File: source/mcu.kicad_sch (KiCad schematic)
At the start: 13 parts

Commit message: Add files via upload
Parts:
- gave numbers to parts that had none: 13
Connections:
- net at C72.1, U11.6 (PH1-OSC_OUT): now also Y1.3
- net PB2: now reaches U11.28 (PB2-BOOT1)
- net PA15: now reaches U11.50 (PA15(JTDI))
- net ADC_15: no longer names the net of U11.25 (PC5(ADC12_IN15))
- net ADC_TEMP2: no longer names the net of U11.26 (PB0(ADC12_IN8))
- net ADC_TEMP3: no longer names the net of U11.27 (PB1(ADC12_IN9))
- net MISO_ADC_EXT2: no longer names the net of U11.22 (PA6(ADC12_IN6))
- net PC10_UART_TX: no longer names the net of U11.51 (PC10)
- net PC11_UART_RX: no longer names the net of U11.52 (PC11)
- net PC12: no longer names the net of U11.53 (PC12)
- net PC9: no longer names the net of U11.40 (PC9)
- net RX_SDA_NSS: no longer names the net of U11.20 (PA4(ADC12_IN4/DAC1_OUT))
- net RX_SDA_NSS: no longer U11.30 (PB11)
- net SCK_ADC_EXT: no longer names the net of U11.21 (PA5(ADC12_IN5/DAC2_OUT))
- net TX_SCL_MOSI: no longer names the net of U11.23 (PA7(ADC12_IN7))
- net TX_SCL_MOSI: no longer U11.29 (PB10)
- no-connect marks 9 -> 20

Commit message: Changes suggested by mxlemming, Elwin and hackey on Discord
New power supplies and using other op-amps for current sense
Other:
- note added: "F-Of-C"
- note removed: "Free-Of-Charge"
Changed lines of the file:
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@@
     (effects (font (size 1.27 1.27)) (justify left bottom))
   )
-  (text "Free-Of-Charge" (at 187.96 191.77 0)
+  (text "F-Of-C" (at 187.96 191.77 0)
     (effects (font (size 2.54 2.54)) (justify left bottom))
   )

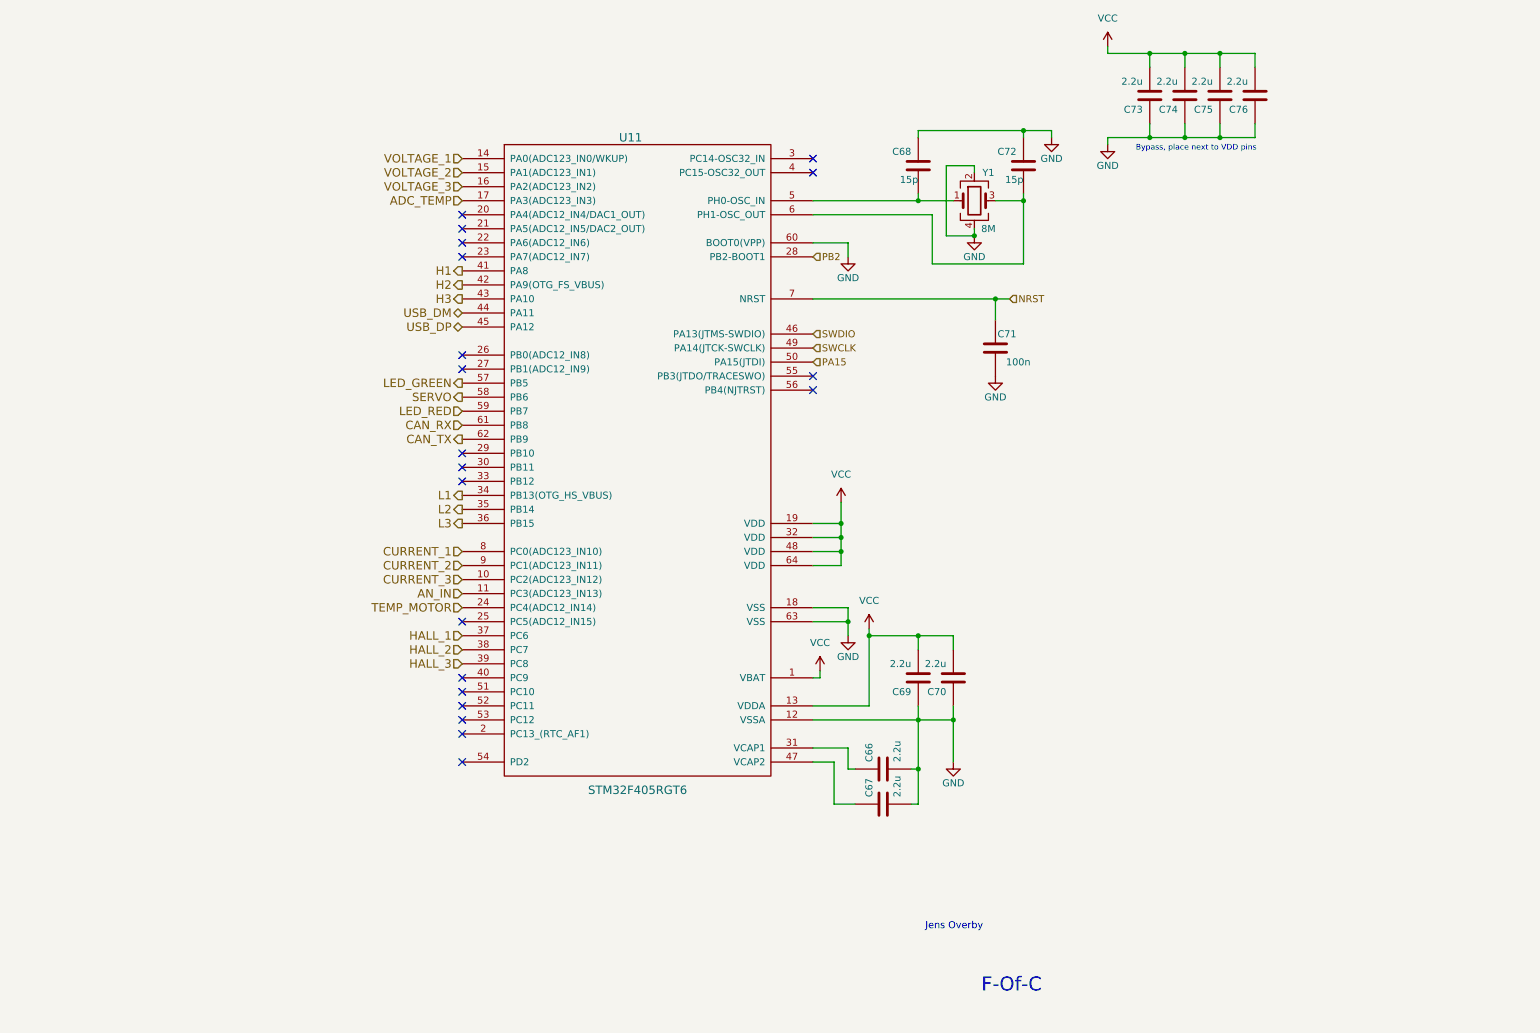
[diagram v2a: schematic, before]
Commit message: First attempt of layout
It's a rats nest. Will have to remove some connections temporarily for the first prototype.
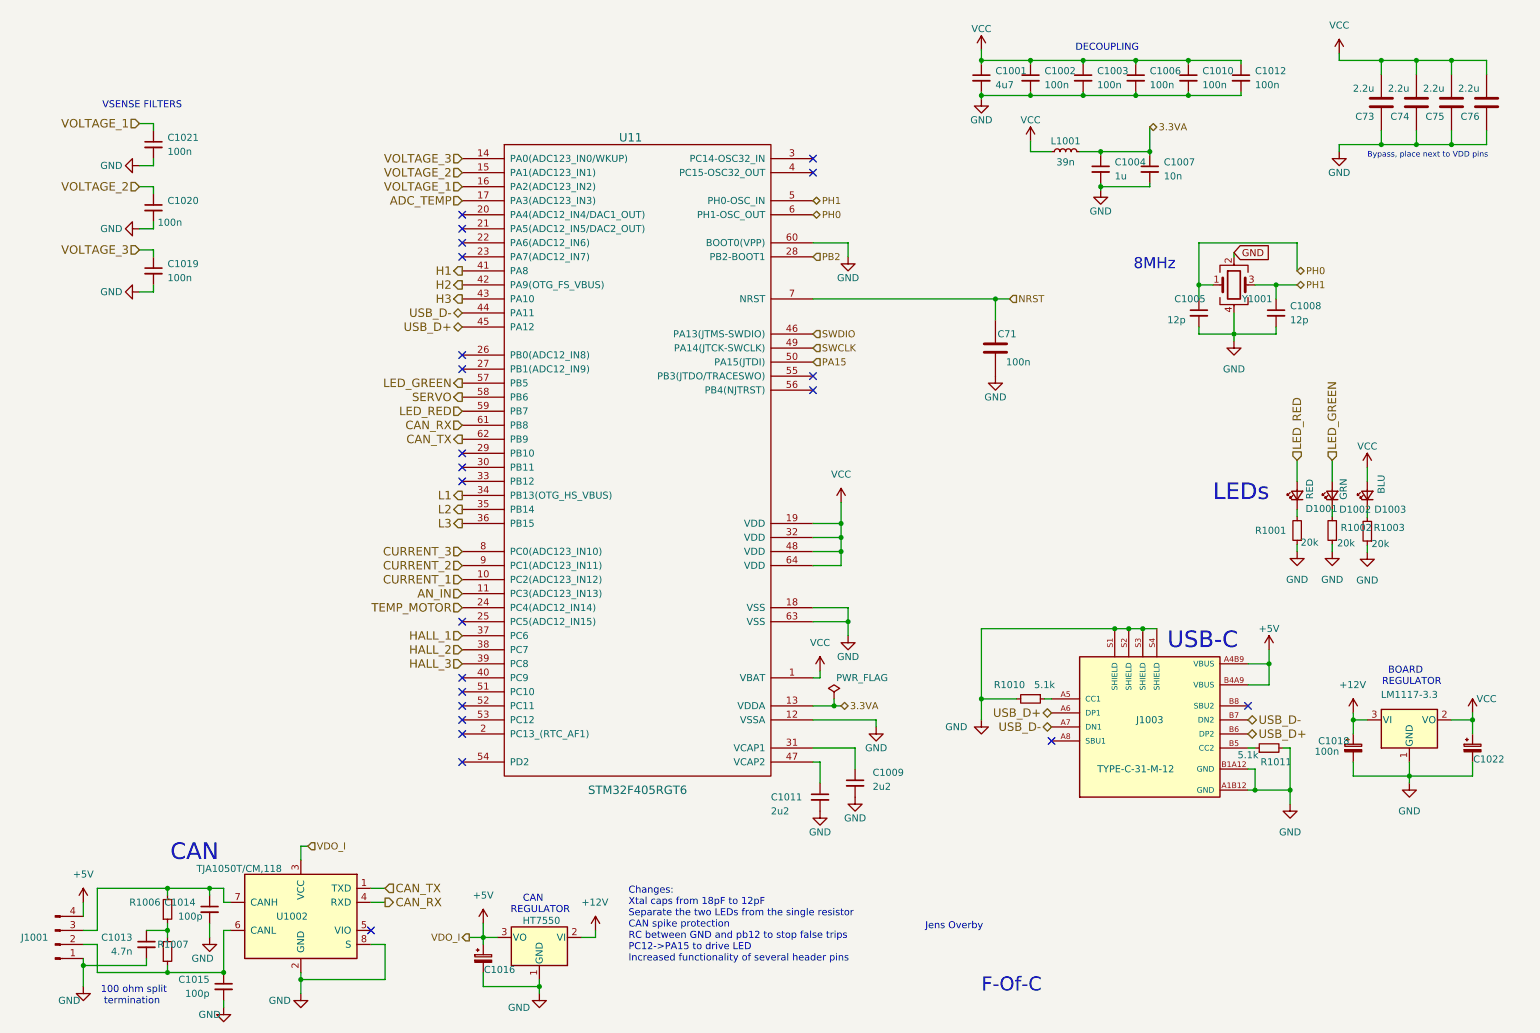
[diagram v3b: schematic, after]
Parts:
- removed C66, C67, C69, C70: 2.2u, Capacitor_SMD:C_0603_1608Metric, symbol BLDC_4-rescue:C-RESCUE-BLDC_4
- removed C68, C72: 15p, Capacitor_SMD:C_0603_1608Metric, symbol BLDC_4-rescue:C-RESCUE-BLDC_4
- removed Y1: 8M, Crystal:Crystal_SMD_3225-4Pin_3.2x2.5mm, symbol Device:Crystal_GND24
- added C1001: 4u7, Capacitor_SMD:C_0402_1005Metric, symbol Device:C_Small
- added C1002, C1003, C1006, C1010, C1012, C1019, C1020, C1021: 100n, Capacitor_SMD:C_0402_1005Metric, symbol Device:C_Small
- added C1004: 1u, Capacitor_SMD:C_0402_1005Metric, symbol Device:C_Small
- added C1005, C1008: 12p, Capacitor_SMD:C_0402_1005Metric, symbol Device:C_Small
- added C1007: 10n, Capacitor_SMD:C_0402_1005Metric, symbol Device:C_Small
- added C1009, C1011: 2u2, Capacitor_SMD:C_0603_1608Metric, symbol Device:C_Small
- added C1013: 4.7n, Capacitor_SMD:C_0402_1005Metric, symbol Device:C_Small
- added C1014, C1015: 100p, Capacitor_SMD:C_0402_1005Metric, symbol Device:C_Small
- added C1016, C1022: 10u, Capacitor_SMD:C_0603_1608Metric, symbol Device:C_Polarized_Small
- added C1018: 100n, Capacitor_Tantalum_SMD:CP_EIA-3216-18_Kemet-A, symbol Device:C_Polarized_Small
- added D1001: RED, LED_SMD:LED_0603_1608Metric, symbol Device:LED_Small
- added D1002: GRN, LED_SMD:LED_0603_1608Metric, symbol Device:LED_Small
- added D1003: BLU, LED_SMD:LED_0603_1608Metric, symbol Device:LED_Small
- added J1001: Conn_01x04_Male, Connector_PinHeader_2.54mm:PinHeader_1x04_P2.54mm_Vertical, symbol Connector:Conn_01x04_Male
- added J1003: TYPE-C-31-M-12, TYPE-C-31-M-12:HRO_TYPE-C-31-M-12, symbol TYPE-C-31-M-12:TYPE-C-31-M-12
- added L1001: 39n, Inductor_SMD:L_0402_1005Metric, symbol Device:L_Small
- added R1001, R1002, R1003: 20k, Resistor_SMD:R_0402_1005Metric, symbol Device:R_Small
- added R1006, R1007: 100Ω, Resistor_SMD:R_0402_1005Metric, symbol Device:R_Small
- added R1010, R1011: 5.1k, Resistor_SMD:R_0402_1005Metric, symbol Device:R_Small
- added U1002: TJA1050T/CM,118, Package_SO:SOIC-8_3.9x4.9mm_P1.27mm, symbol Interface_CAN_LIN:TJA1051T-3
- added U1003: HT7550, Package_TO_SOT_SMD:SOT-89-3, symbol Regulator_Linear:L79L08_SOT89
- added U1005: LM1117-3.3, Package_TO_SOT_SMD:SOT-223-3_TabPin2, symbol Regulator_Linear:LM1117-3.3
- added Y1001: Crystal_GND24, Crystal:Crystal_SMD_3225-4Pin_3.2x2.5mm, symbol Device:Crystal_GND24
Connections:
- net CAN_RX: now also U1002.4 (RXD)
- net CAN_TX: now also U1002.1 (TXD)
- net CURRENT_1: now also U11.10 (PC2(ADC123_IN12)); no longer U11.8 (PC0(ADC123_IN10))
- net CURRENT_3: now also U11.8 (PC0(ADC123_IN10)); no longer U11.10 (PC2(ADC123_IN12))
- net GND: now also C1001.2, C1002.2, C1003.2, C1004.2, C1005.2, C1006.2, C1007.2, C1008.2, C1009.2, C1010.2, C1011.2, C1012.2, C1013.2, C1014.2, C1015.2, C1016.2, C1018.2, C1019.2, C1020.2, C1021.2, C1022.2, J1001.1 (Pin_1), J1003.A1B12 (GND), J1003.B1A12 (GND), J1003.S1 (SHIELD), J1003.S2 (SHIELD), J1003.S3 (SHIELD), J1003.S4 (SHIELD), R1001.1, R1002.1, R1003.1, R1010.2, R1011.2, U1002.2 (GND), U1002.8 (S), U1003.1 (GND), U1005.1 (GND), Y1001.2, Y1001.4
- net LED_GREEN: now also D1002.2 (A)
- net LED_RED: now also D1001.2 (A)
- net VCC: now also C1001.1, C1002.1, C1003.1, C1006.1, C1010.1, C1012.1, C1022.1, D1003.2 (A), L1001.1, U1005.2 (VO); no longer U11.13 (VDDA)
- net VOLTAGE_1: now also U11.16 (PA2(ADC123_IN2)), C1021.1; no longer U11.14 (PA0(ADC123_IN0/WKUP))
- net VOLTAGE_2: now also C1020.1
- net VOLTAGE_3: now also U11.14 (PA0(ADC123_IN0/WKUP)), C1019.1; no longer U11.16 (PA2(ADC123_IN2))
- net at U11.47 (VCAP2): now also C1011.1
- net PH0: now reaches U11.6 (PH1-OSC_OUT)
- net PH0: now also C1005.1, Y1001.1
- net PH1: now reaches U11.5 (PH0-OSC_IN)
- net PH1: now also C1008.1, Y1001.3
- net at U11.31 (VCAP1): now also C1009.1
- net USB_DM renamed USB_D-
- net USB_D-: now also J1003.A7 (DN1), J1003.B7 (DN2)
- net USB_DP renamed USB_D+
- net USB_D+: now also J1003.A6 (DP1), J1003.B6 (DP2)
- new net: C1015.1, J1001.2 (Pin_2), R1007.1, U1002.6 (CANL)
- new net: C1014.1, J1001.3 (Pin_3), R1006.2, U1002.7 (CANH)
- new net: C1013.1, R1006.1, R1007.2
- new net: D1001.1 (K), R1001.2
- new net: J1003.A5 (CC1), R1010.1
- new net: D1002.1 (K), R1002.2
- new net: J1003.B5 (CC2), R1011.1
- new net: D1003.1 (K), R1003.2
- new net +12V: C1018.1, U1003.2 (VI), U1005.3 (VI)
- new net +5V: C1016.1, J1001.4 (Pin_4), J1003.A4B9 (VBUS), J1003.B4A9 (VBUS), U1002.3 (VCC), U1003.3 (VO)
- new net 3.3VA: C1004.1, C1007.1, L1001.2, U11.13 (VDDA)
- no-connect marks 20 -> 23
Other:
- note added: "100 ohm split termination"
- note added: "8MHz"
- note added: "BOARD REGULATOR"
- note added: "CAN"
- note added: "CAN REGULATOR"
- note added: "Changes: Xtal caps from 18pF to 12pF Separate the two LEDs from the single resistor CAN spike protection RC between GND and pb12 to stop false trips PC12->PA15 to drive LED Increased functionality of several header pins"
- note added: "DECOUPLING"
- note added: "LEDs"
- note added: "USB-C"
- note added: "VSENSE FILTERS"
- moved on the sheet: C73, C74, C75, C76

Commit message: Most components now jlcpcb basic
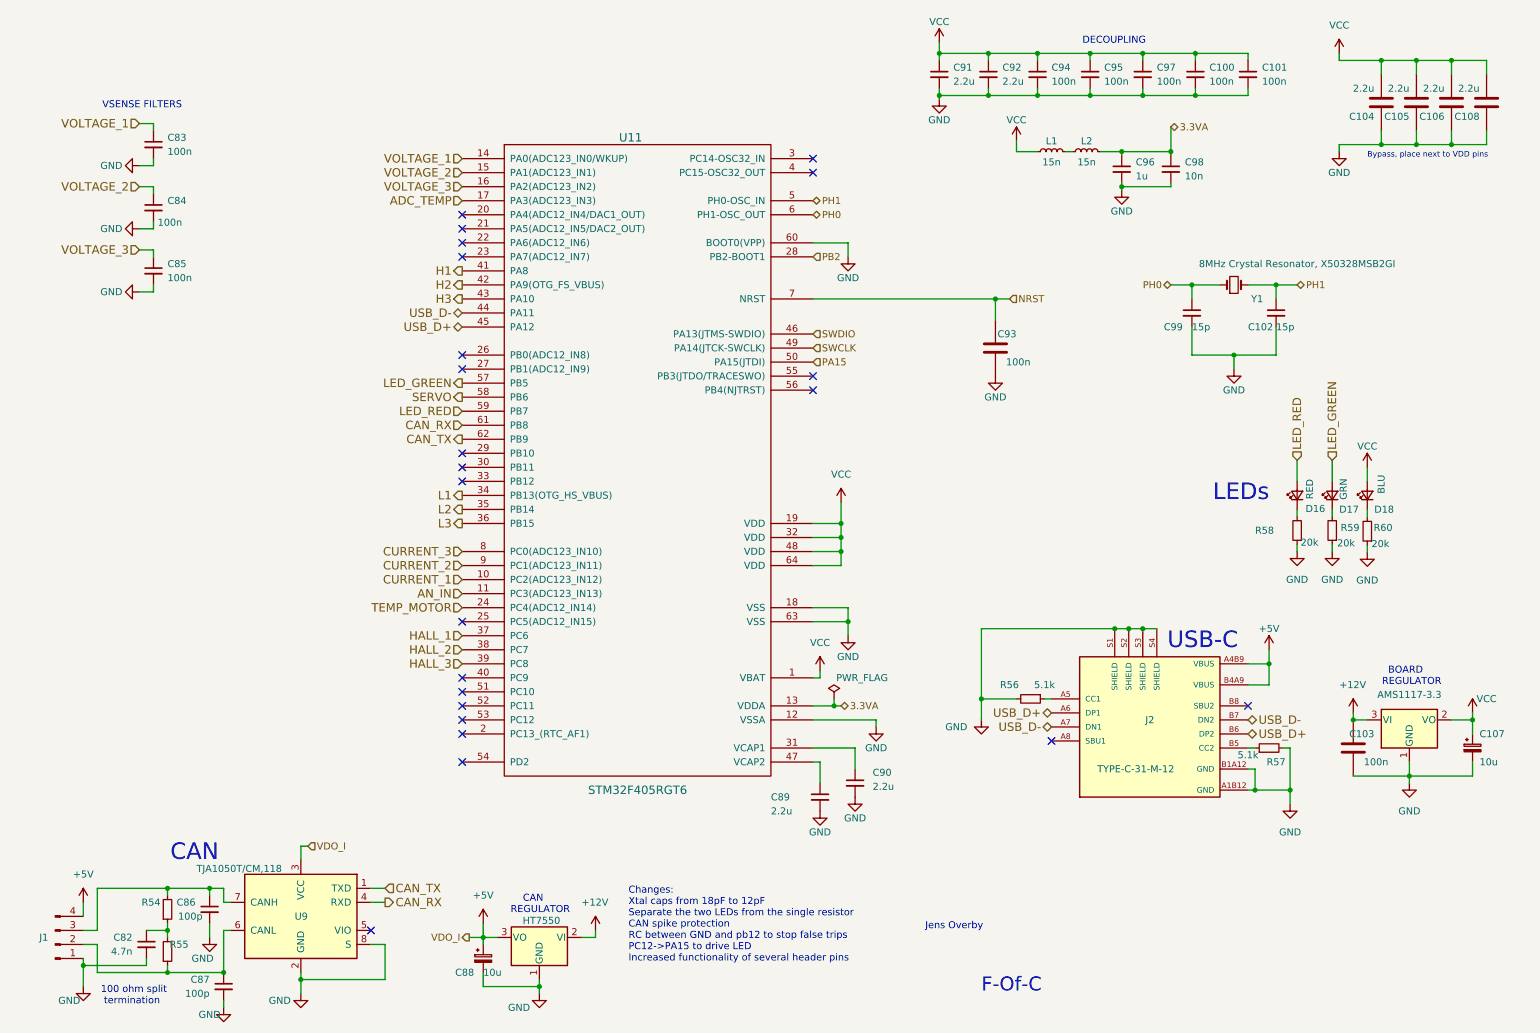
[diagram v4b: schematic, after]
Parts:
- removed C1018: 100n, Capacitor_Tantalum_SMD:CP_EIA-3216-18_Kemet-A, symbol Device:C_Polarized_Small
- added C103: 100n, Capacitor_SMD:C_0402_1005Metric, symbol BLDC_4-rescue:C-RESCUE-BLDC_4
- added C92: 2.2u, Capacitor_SMD:C_0603_1608Metric, symbol Device:C_Small
- added L2: 15n, Inductor_SMD:L_0402_1005Metric, symbol Device:L_Small
- C102: renamed from C1008; value 12p -> 15p; LCSC C1547 -> C1548
- C104: renamed from C73; LCSC (none) -> C23630
- C105: renamed from C74; LCSC (none) -> C23630
- C106: renamed from C75; LCSC (none) -> C23630
- C107: renamed from C1022; footprint Capacitor_SMD:C_0603_1608Metric -> Capacitor_Tantalum_SMD:CP_EIA-3216-10_Kemet-I; LCSC C962635 -> C7171
- C108: renamed from C76; LCSC (none) -> C23630
- C88: renamed from C1016; footprint Capacitor_SMD:C_0603_1608Metric -> Capacitor_Tantalum_SMD:CP_EIA-3216-10_Kemet-I_Pad1.58x1.35mm_HandSolder; LCSC C962635 -> C7171
- C89: renamed from C1011; value 2u2 -> 2.2u
- C90: renamed from C1009; value 2u2 -> 2.2u
- C91: renamed from C1001; value 4u7 -> 2.2u; footprint Capacitor_SMD:C_0402_1005Metric -> Capacitor_SMD:C_0603_1608Metric; LCSC C23733 -> C23630
- C93: renamed from C71; footprint Capacitor_SMD:C_0603_1608Metric -> Capacitor_SMD:C_0402_1005Metric; LCSC (none) -> C1525
- C99: renamed from C1005; value 12p -> 15p; LCSC C1547 -> C1548
- L1: renamed from L1001; value 39n -> 15n; LCSC C26443 -> C27143
- R56: renamed from R1010; LCSC C105872 -> C25905
- R57: renamed from R1011; LCSC C105872 -> C25905
- U12: renamed from U1005; value LM1117-3.3 -> AMS1117-3.3; LCSC C126027 -> C6186
- Y1: renamed from Y1001; value Crystal_GND24 -> 8MHz Crystal Resonator, X50328MSB2GI; footprint Crystal:Crystal_SMD_3225-4Pin_3.2x2.5mm -> Crystal:Crystal_SMD_5032-2Pin_5.0x3.2mm; symbol Device:Crystal_GND24 -> Device:Crystal_Small; LCSC C518154 -> C115962; MANUFACTURER Suzhou Liming Elec -> (none)
- renumbered C1010 to C100, C1012 to C101, C1013 to C82, C1021 to C83, C1020 to C84, C1019 to C85, C1014 to C86, C1015 to C87, C1002 to C94, C1003 to C95, C1004 to C96, C1006 to C97, C1007 to C98, D1001 to D16, D1002 to D17, D1003 to D18, J1001 to J1, J1003 to J2, R1006 to R54, R1007 to R55, R1001 to R58, R1002 to R59, R1003 to R60, U1003 to U10, U1002 to U9
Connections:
- net +12V: now also C103.2
- net 3.3VA: now also L2.2; no longer L1.2
- net GND: now also C103.1, C92.2; no longer Y1.2, Y1.4
- net PH1: now also Y1.2; no longer Y1.3
- net VCC: now also C92.1
- net VOLTAGE_1: now also U11.14 (PA0(ADC123_IN0/WKUP)); no longer U11.16 (PA2(ADC123_IN2))
- net VOLTAGE_3: now also U11.16 (PA2(ADC123_IN2)); no longer U11.14 (PA0(ADC123_IN0/WKUP))
- new net: L1.2, L2.1
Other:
- note removed: "8MHz"
- moved on the sheet: C100, C101, C91, C94, C95, C96, C97, C98, C99, L1

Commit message: Add files via upload
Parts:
- removed L2: 15n, Inductor_SMD:L_0402_1005Metric, symbol Device:L_Small
- C100, C101, C103, C83, C84, C85, C93, C94, C95, C97: footprint Capacitor_SMD:C_0402_1005Metric -> Capacitor_SMD:C_0603_1608Metric; LCSC C1525 -> C14663
- C102, C99: footprint Capacitor_SMD:C_0402_1005Metric -> Capacitor_SMD:C_0603_1608Metric; LCSC C1548 -> C1644
- C82: footprint Capacitor_SMD:C_0402_1005Metric -> Capacitor_SMD:C_0603_1608Metric; LCSC C1538 -> C53987
- C86, C87: footprint Capacitor_SMD:C_0402_1005Metric -> Capacitor_SMD:C_0603_1608Metric; LCSC C1546 -> C14858
- C96: footprint Capacitor_SMD:C_0402_1005Metric -> Capacitor_SMD:C_0603_1608Metric; LCSC C52923 -> C15849
- C98: footprint Capacitor_SMD:C_0402_1005Metric -> Capacitor_SMD:C_0603_1608Metric; LCSC C15195 -> C57112
- L1: value 15n -> 30n; footprint Inductor_SMD:L_0402_1005Metric -> Inductor_SMD:L_0603_1608Metric; LCSC C27143 -> C280269
- R53: renamed from R54; footprint Resistor_SMD:R_0402_1005Metric -> Resistor_SMD:R_0603_1608Metric; LCSC C25076 -> C22775
- R54: renamed from R55; footprint Resistor_SMD:R_0402_1005Metric -> Resistor_SMD:R_0603_1608Metric; LCSC C25076 -> C22775
- R55: renamed from R56; footprint Resistor_SMD:R_0402_1005Metric -> Resistor_SMD:R_0603_1608Metric; LCSC C25905 -> C23186
- R56: renamed from R57; footprint Resistor_SMD:R_0402_1005Metric -> Resistor_SMD:R_0603_1608Metric; LCSC C25905 -> C23186
- R57: renamed from R58; footprint Resistor_SMD:R_0402_1005Metric -> Resistor_SMD:R_0603_1608Metric; LCSC C25765 -> C4184
- R58: renamed from R59; footprint Resistor_SMD:R_0402_1005Metric -> Resistor_SMD:R_0603_1608Metric; LCSC C25765 -> C4184
- R59: renamed from R60; footprint Resistor_SMD:R_0402_1005Metric -> Resistor_SMD:R_0603_1608Metric; LCSC C25765 -> C4184
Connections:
- net 3.3VA: now also L1.2
- net AN_IN: now also U11.14 (PA0(ADC123_IN0/WKUP)); no longer U11.11 (PC3(ADC123_IN13))
- net CURRENT_1: now also U11.16 (PA2(ADC123_IN2)); no longer U11.10 (PC2(ADC123_IN12))
- net CURRENT_2: now also U11.11 (PC3(ADC123_IN13)); no longer U11.9 (PC1(ADC123_IN11))
- net VOLTAGE_1: now also U11.15 (PA1(ADC123_IN1)); no longer U11.14 (PA0(ADC123_IN0/WKUP))
- net VOLTAGE_2: now also U11.10 (PC2(ADC123_IN12)); no longer U11.15 (PA1(ADC123_IN1))
- net VOLTAGE_3: now also U11.9 (PC1(ADC123_IN11)); no longer U11.16 (PA2(ADC123_IN2))
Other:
- moved on the sheet: C93
